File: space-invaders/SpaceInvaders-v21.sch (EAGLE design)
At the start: 27 parts, among them J2-J4 TM4C123GXL, J3-J1 TM4C123GXL, J5 NOKIA_5110, J6 NOKIA_5110, J7 9V, U1 LM7805CT

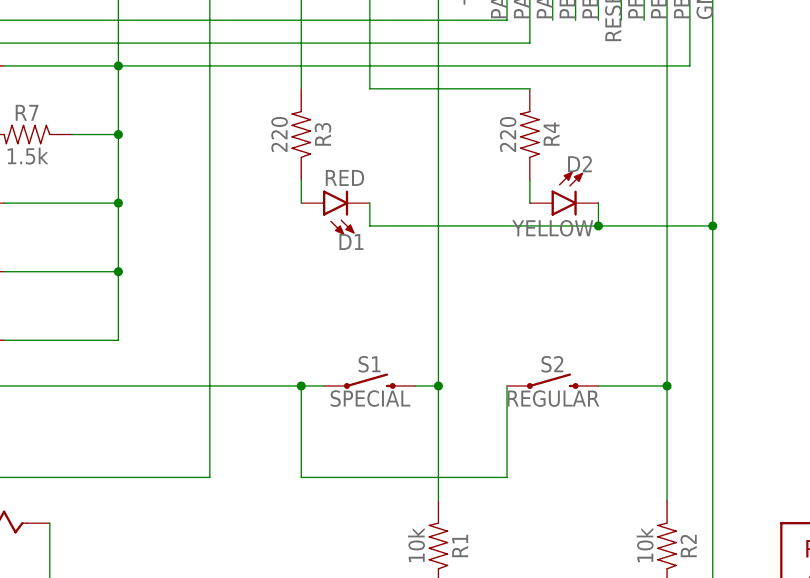
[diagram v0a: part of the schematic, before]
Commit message: Add GND to RATSNEST
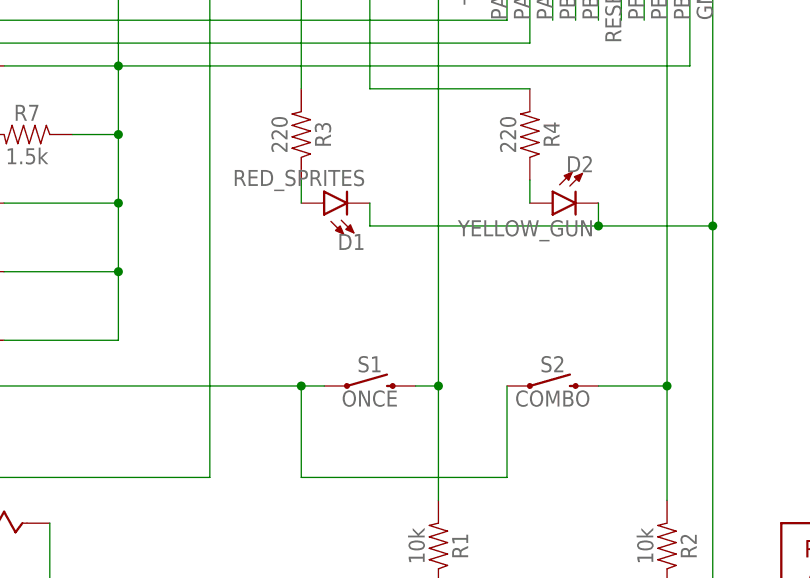
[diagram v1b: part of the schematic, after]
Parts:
- D1: value RED -> RED_SPRITES
- D2: value YELLOW -> YELLOW_GUN
- S1: value SPECIAL -> ONCE
- S2: value REGULAR -> COMBO
- U1: device SparkFun-IC-Power:V_REG_78XX-TO-220 -> SparkFun-IC-Power:V_REG_78XXSINK
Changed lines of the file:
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@@
 <?xml version="1.0" encoding="utf-8"?>
 <!DOCTYPE eagle SYSTEM "eagle.dtd">
-<eagle version="8.0.2">
+<eagle version="8.1.0">
 <drawing>
 <settings>
@@
 </variantdefs>
 <classes>
-<class number="0" name="default" width="0.254" drill="0.508">
-<clearance class="0" value="0.254"/>
-</class>
-<class number="1" name="power" width="0.3048" drill="0.508">
-<clearance class="1" value="0.254"/>
+<class number="0" name="default" width="0.4064" drill="0">
 </class>
 </classes>
@@
 <part name="LS1" library="SparkFun-Electromechanical" deviceset="BUZZER" device="-PTH" value="BUZZER"/>
 <part name="VR1" library="SparkFun-Resistors" deviceset="POTENTIOMETER_SLIDE" device="-30MM-1/10W-20%" value="10k"/>
-<part name="D1" library="SparkFun-LED" deviceset="LED" device="5MM" value="RED"/>
-<part name="D2" library="SparkFun-LED" deviceset="LED" device="5MM" value="YELLOW"/>
+<part name="D1" library="SparkFun-LED" deviceset="LED" device="5MM" value="RED_SPRITES"/>
+<part name="D2" library="SparkFun-LED" deviceset="LED" device="5MM" value="YELLOW_GUN"/>
 <part name="R1" library="SparkFun-Resistors" deviceset="10KOHM" device="-HORIZ-1/4W-5%" value="10k"/>
 <part name="R2" library="SparkFun-Resistors" deviceset="10KOHM" device="-HORIZ-1/4W-5%" value="10k"/>
@@
 <part name="C1" library="SparkFun-Capacitors" deviceset="0.1UF" device="-KIT-EZ-50V-20%" value="0.1uF"/>
 <part name="C2" library="SparkFun-Capacitors" deviceset="0.1UF" device="-KIT-EZ-50V-20%" value="0.33uF"/>
-<part name="U1" library="SparkFun-IC-Power" deviceset="V_REG_78XX" device="-TO-220" value="LM7805CT"/>
+<part name="U1" library="SparkFun-IC-Power" deviceset="V_REG_78XX" device="SINK" value="LM7805CT"/>
 <part name="FRAME1" library="SparkFun-Aesthetics" deviceset="FRAME-LETTER" device=""/>
 <part name="J7" library="SparkFun-Connectors" deviceset="BC9VPC" device="" value="9V"/>
-<part name="S1" library="SparkFun-Switches" deviceset="MOMENTARY-SWITCH-SPST" device="-PTH-6.0MM" value="SPECIAL"/>
-<part name="S2" library="SparkFun-Switches" deviceset="MOMENTARY-SWITCH-SPST" device="-PTH-6.0MM" value="REGULAR"/>
+<part name="S1" library="SparkFun-Switches" deviceset="MOMENTARY-SWITCH-SPST" device="-PTH-6.0MM" value="ONCE"/>
+<part name="S2" library="SparkFun-Switches" deviceset="MOMENTARY-SWITCH-SPST" device="-PTH-6.0MM" value="COMBO"/>
 <part name="S3" library="SparkFun-Switches" deviceset="SWITCH-SPDT" device="-PTH-11.6X4.0MM" value="POWER_SWITCH"/>
 </parts>
@@
 </segment>
 </net>
-<net name="VIN" class="1">
+<net name="VIN" class="0">
 <segment>
 <pinref part="U1" gate="G$1" pin="IN"/>
@@
 </segment>
 </net>
-<net name="VBUS" class="1">
+<net name="VBUS" class="0">
 <segment>
 <pinref part="U1" gate="G$1" pin="OUT"/>
@@
 </segment>
 </net>
-<net name="3.3V" class="1">
+<net name="3.3V" class="0">
 <segment>
 <pinref part="J3-J1" gate="G$1" pin="20"/>
@@
 </segment>
 </net>
-<net name="9V" class="1">
+<net name="9V" class="0">
 <segment>
 <pinref part="J7" gate="G$1" pin="V+"/>
